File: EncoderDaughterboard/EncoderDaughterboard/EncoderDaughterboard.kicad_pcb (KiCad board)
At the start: 2 copper layers, 54 x 54 mm, 36 parts, among them J1 JST-SH-4, J2 USB_BOOT, J3 RST, J4 JST-SH-4, J5 Conn_01x03, U1 RP2040, U2 NCP1117-3.3_SOT223, U3 W25Q128JVS, U4 TMC6300, Y1 Crystal_Small

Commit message: Val pls dxf
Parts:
- removed J5: Conn_01x03, Connector_JST:JST_GH_SM03B-GHS-TB_1x03-1MP_P1.25mm_Horizontal
- removed R7, R8: 10k, Resistor_SMD:R_0402_1005Metric
- removed R9: 1k, Resistor_SMD:R_0402_1005Metric
- added C19: 22uf, Capacitor_SMD:C_0402_1005Metric, F.Cu at (126.0, 43.5)
- added C20: 10nf, Capacitor_SMD:C_0402_1005Metric, F.Cu at (126.0, 45.4)
- added C21: 22uf, Capacitor_SMD:C_0402_1005Metric, F.Cu at (126.0, 47.4)
- added C22: 22uf, Capacitor_SMD:C_0402_1005Metric, F.Cu at (128.9, 35.6)
- added C23: 22uf, Capacitor_SMD:C_0402_1005Metric, F.Cu at (128.9, 37.6)
- added C24: 0.1uf, Capacitor_SMD:C_0402_1005Metric, F.Cu at (128.9, 39.5)
- added C25: 0.1uf, Capacitor_SMD:C_0402_1005Metric, F.Cu at (128.9, 41.5)
- added C26: 22uf, Capacitor_SMD:C_0402_1005Metric, F.Cu at (128.9, 43.5)
- added L1: 1.0uH, Inductor_SMD:L_0805_2012Metric, F.Cu at (130.9, 59.0)
- added R10: 402k, Resistor_SMD:R_0402_1005Metric, F.Cu at (143.5, 43.9)
- added R11: 1M, Resistor_SMD:R_0402_1005Metric, F.Cu at (143.5, 45.8)
- added R12: 100k, Resistor_SMD:R_0402_1005Metric, F.Cu at (143.5, 47.8)
- added R13: 4.7k, Resistor_SMD:R_0402_1005Metric, F.Cu at (62.5, 73.6)
- added R14: 4.7k, Resistor_SMD:R_0402_1005Metric, F.Cu at (62.5, 71.6)
- added R6: Rsense, Resistor_SMD:R_0402_1005Metric, F.Cu at (140.6, 53.8)
- added U5: TPS61230DRC, Package_SON:Texas_S-PVSON-N10_ThermalVias, F.Cu at (141.8, 57.5)
- added U6: TPS2041B, Package_TO_SOT_SMD:SOT-23-5, F.Cu at (121.4, 57.4)
- C13: value 100nf -> C_Small
- J1, J4: moved to F.Cu
- J2: footprint Connector_PinSocket_1.27mm:PinSocket_1x02_P1.27mm_Vertical -> Connector_PinHeader_1.00mm:PinHeader_1x02_P1.00mm_Horizontal
- J3: footprint Connector_Wire:SolderWire-0.5sqmm_1x02_P4.6mm_D0.9mm_OD2.1mm -> Connector_PinHeader_1.00mm:PinHeader_1x02_P1.00mm_Horizontal
- U1: footprint RP2040:QFN40P700X700X90-57N -> RP2040D:QFN40P700X700X90-57N
- U4: footprint TMC6300:QFN20_3x3_TRI -> footprints:QFN20_3x3_TRI
- Y1: value Crystal_Small -> 12MHz
- moved J2 92.9 mm to (155.7, 30.0)
- moved U2 88.6 mm to (135.1, 31.0)
- moved J1 78.2 mm to (156.9, 58.0), turned to -90 degrees
- moved R1 66.0 mm to (140.6, 43.9)
- moved R2 66.0 mm to (140.6, 45.8)
- moved R3 66.0 mm to (140.6, 47.8)
- moved R4 62.0 mm to (140.6, 49.8)
- moved C1 61.8 mm to (120.3, 35.6)
- moved C13 61.8 mm to (123.2, 45.4)
- moved C2 61.8 mm to (120.3, 37.6)
- moved C17 61.8 mm to (126.0, 39.5)
- moved C18 61.8 mm to (126.0, 41.5)
- moved U4 54.9 mm to (71.6, 87.3)
- moved J4 49.6 mm to (57.7, 72.6)
- moved C10 47.3 mm to (123.2, 39.5), turned to 0 degrees
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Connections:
- J4 pad 2: I2C_SDL -> I2C_SCL
- U1 pad 16: unconnected-(U1-GPIO13-Pad16) -> I2C_SDA
- U1 pad 17: unconnected-(U1-GPIO14-Pad17) -> I2C_SCL
- U1 pad 27: unconnected-(U1-GPIO16-Pad27) -> /TMC_UH
- U1 pad 28: unconnected-(U1-GPIO17-Pad28) -> /TMC_UL
- U1 pad 29: unconnected-(U1-GPIO18-Pad29) -> /TMC_VH
- U1 pad 30: unconnected-(U1-GPIO19-Pad30) -> /TMC_VL
- U1 pad 31: unconnected-(U1-GPIO20-Pad31) -> /TMC_WH
- U1 pad 32: unconnected-(U1-GPIO21-Pad32) -> /TMC_WL
- U1 pad 34: unconnected-(U1-GPIO22-Pad34) -> /TMC_DIAG
- U4 pad 1: MOTOR_W -> BLDC_W
- U4 pad 11: Net-(Q1-D) -> DRV_VIO
- U4 pad 15: MOTOR_U -> BLDC_U
- U4 pad 17: MOTOR_V -> BLDC_V
- U4 pad 21: unconnected-(U4-PAD-Pad21) -> (no net)
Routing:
- net /QSPI_SD3: track 25.0 -> 0.00 mm
- net /QSPI_SCLK: track 21.9 -> 0.00 mm
- net Net-(J3-Pin_2): track 0.00 -> 18.9 mm
- net /QSPI_SD0: track 18.7 -> 0.00 mm
- net I2C_SDA: track 0.00 -> 17.6 mm
- net /TMC_UH: track 0.00 -> 17.6 mm
- net I2C_SCL: track 0.00 -> 17.4 mm
- net /TMC_UL: track 0.00 -> 17.1 mm, vias 0 -> 2
- net +3V3: track 15.0 -> 1.54 mm
- net /QSPI_SD2: track 6.28 -> 0.00 mm
- net +1V1: track 6.07 -> 0.00 mm
- net Net-(U1-XOUT): track 1.70 -> 6.68 mm
- net /QSPI_SD1: track 4.84 -> 0.00 mm
- net Net-(U4-BRUV): track 4.60 -> 0.00 mm, vias 2 -> 0
- net /QSPI_SS: track 3.39 -> 0.00 mm
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
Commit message: The Spaghetti has been cooked
I am so sorry
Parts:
- moved J2 87.8 mm to (90.3, 88.5), turned to -90 degrees
- moved C24 78.9 mm to (66.0, 87.2)
- moved U2 75.4 mm to (70.8, 70.4)
- moved R6 74.9 mm to (74.5, 89.2), turned to 180 degrees
- moved C25 73.5 mm to (69.5, 84.8), turned to -90 degrees
- moved L1 71.9 mm to (59.5, 67.8), turned to 180 degrees
- moved C26 71.6 mm to (70.5, 84.8), turned to 90 degrees
- moved R1 70.9 mm to (82.3, 84.1)
- moved R11 70.8 mm to (76.8, 69.4)
- moved R10 70.2 mm to (77.8, 68.4)
- moved R2 69.2 mm to (82.3, 83.1)
- moved R12 67.1 mm to (79.7, 68.4)
- moved C16 66.9 mm to (81.5, 87.5), turned to 90 degrees
- moved J1 66.6 mm to (97.2, 87.4), turned to 180 degrees
- moved C11 65.6 mm to (71.1, 81.5)
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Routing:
- net +3V3: track 1.54 -> 77.0 mm, vias 0 -> 10
- net VBUS: track 0.00 -> 73.3 mm, vias 0 -> 2
- net +5V: track 0.00 -> 54.7 mm, vias 0 -> 4
- net /QSPI_SS: track 0.00 -> 23.7 mm
- net Net-(L1-Pad2): track 0.00 -> 21.0 mm
- net +1V1: track 0.00 -> 19.8 mm, vias 0 -> 2
- net D+: track 0.00 -> 17.9 mm, vias 0 -> 2
- net /TMC_DIAG: track 0.00 -> 17.2 mm, vias 0 -> 2
- net /QSPI_SD1: track 0.00 -> 16.7 mm
- net D-: track 0.00 -> 15.9 mm, vias 0 -> 2
- net /TMC_WL: track 0.00 -> 15.4 mm, vias 0 -> 2
- net GND: track 0.00 -> 14.4 mm, vias 0 -> 33
- net /TMC_VL: track 0.00 -> 13.4 mm, vias 0 -> 2
- net /QSPI_SD2: track 0.00 -> 12.9 mm
- net /TMC_UL: track 17.1 -> 7.62 mm
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- added copper zone on B.Cu, net GND
- added copper zone on F.Cu, net GND
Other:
- outline, holes or cut-outs redrawn

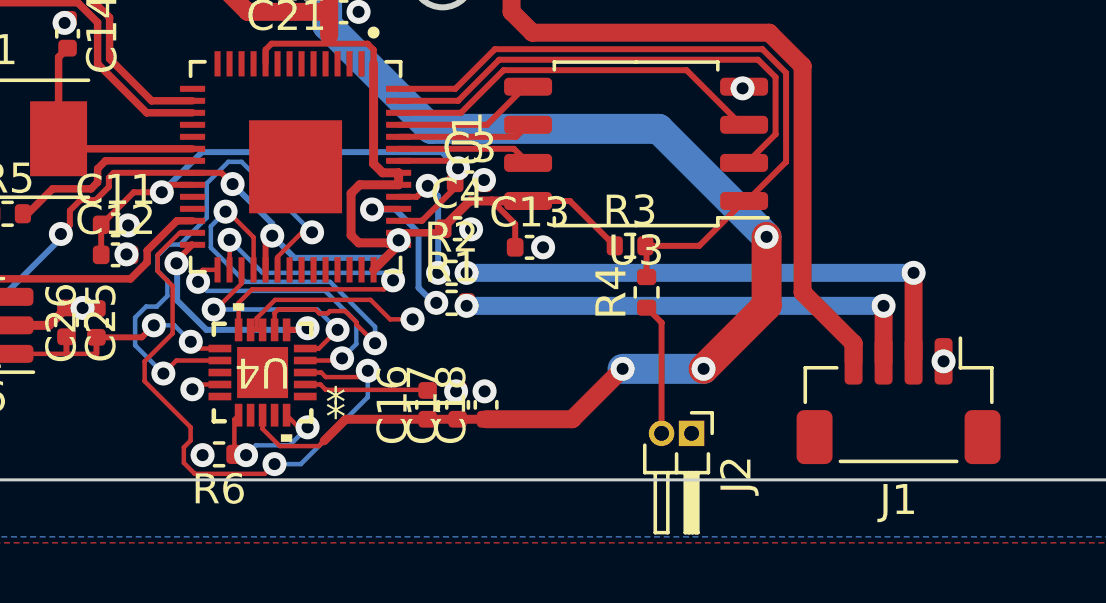
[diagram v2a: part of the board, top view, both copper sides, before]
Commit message: added motor conection VIAs
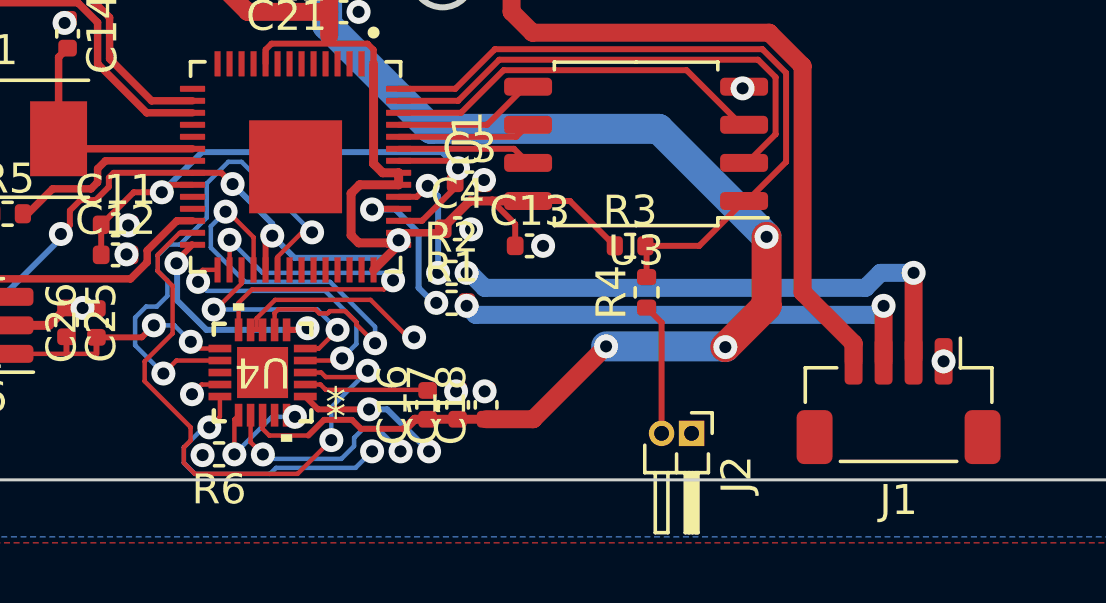
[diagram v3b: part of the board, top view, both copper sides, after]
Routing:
- net BLDC_U: track 0.00 -> 9.55 mm, vias 0 -> 2
- net BLDC_V: track 0.00 -> 7.04 mm, vias 0 -> 2
- net BLDC_W: track 0.00 -> 5.14 mm, vias 0 -> 2
- net Net-(U4-BRUV): track 5.06 -> 4.20 mm

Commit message: over 100 DRC errors but hey weve got a render!
:sleepdepriveddylan:
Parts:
- added J5: Conn_01x03, Connector_PinHeader_1.27mm:PinHeader_1x03_P1.27mm_Vertical, F.Cu at (85.4, 88.4)
- moved C16 1.68 mm to (82.0, 85.9)
- moved C17 1.68 mm to (83.0, 85.9)
- moved C18 1.68 mm to (84.0, 85.9)
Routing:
- net GND: track 14.8 -> 22.0 mm, vias 33 -> 32
- net BLDC_W: track 5.14 -> 9.23 mm, vias 2 -> 1
- net BLDC_V: track 7.04 -> 10.6 mm, vias 2 -> 1
- net BLDC_U: track 9.55 -> 13.0 mm, vias 2 -> 1
- net Net-(U4-VCP): track 4.16 -> 5.70 mm
- net Net-(L1-Pad2): track 21.0 -> 21.9 mm
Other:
- outline, holes or cut-outs redrawn
